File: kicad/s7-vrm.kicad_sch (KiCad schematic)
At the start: 33 parts, among them J1 Conn_02x15_Row_Letter_First, Q1 Q_NPN_BEC, Q2 Q_NMOS_GDS, Q3 Q_NMOS_GDS, SW1 SW_DIP_x04, U1 NCP1579

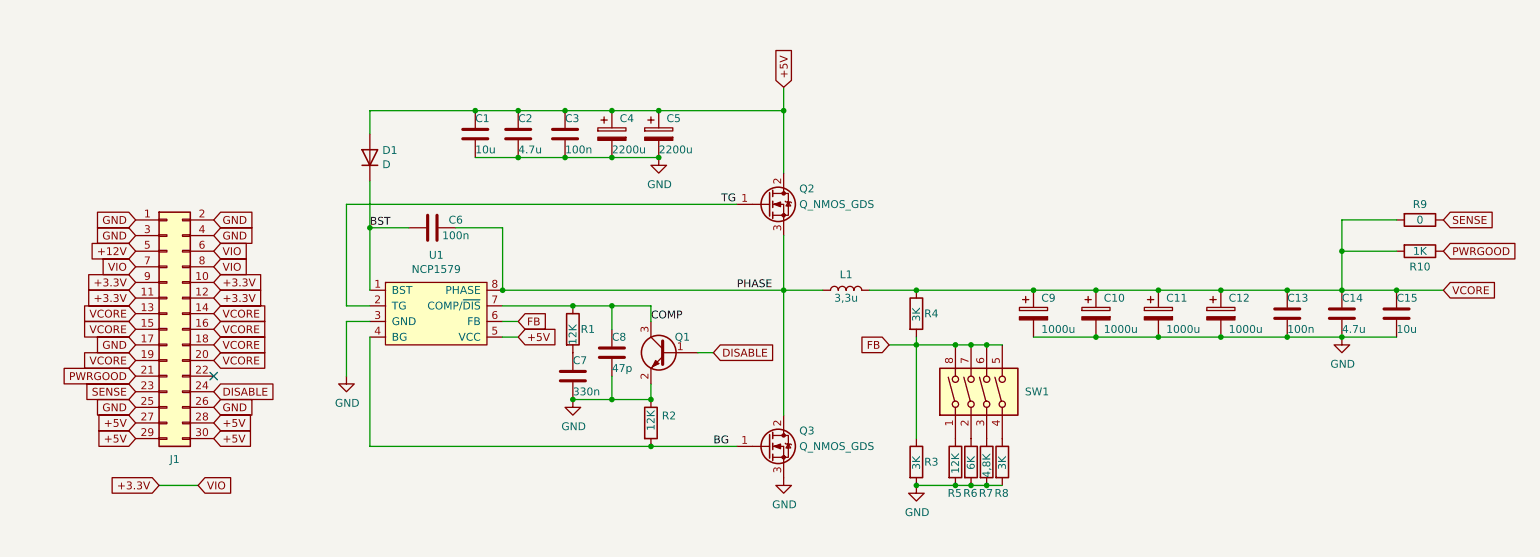
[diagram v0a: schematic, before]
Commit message: Using sence to FB and transistor for PWRGOOD
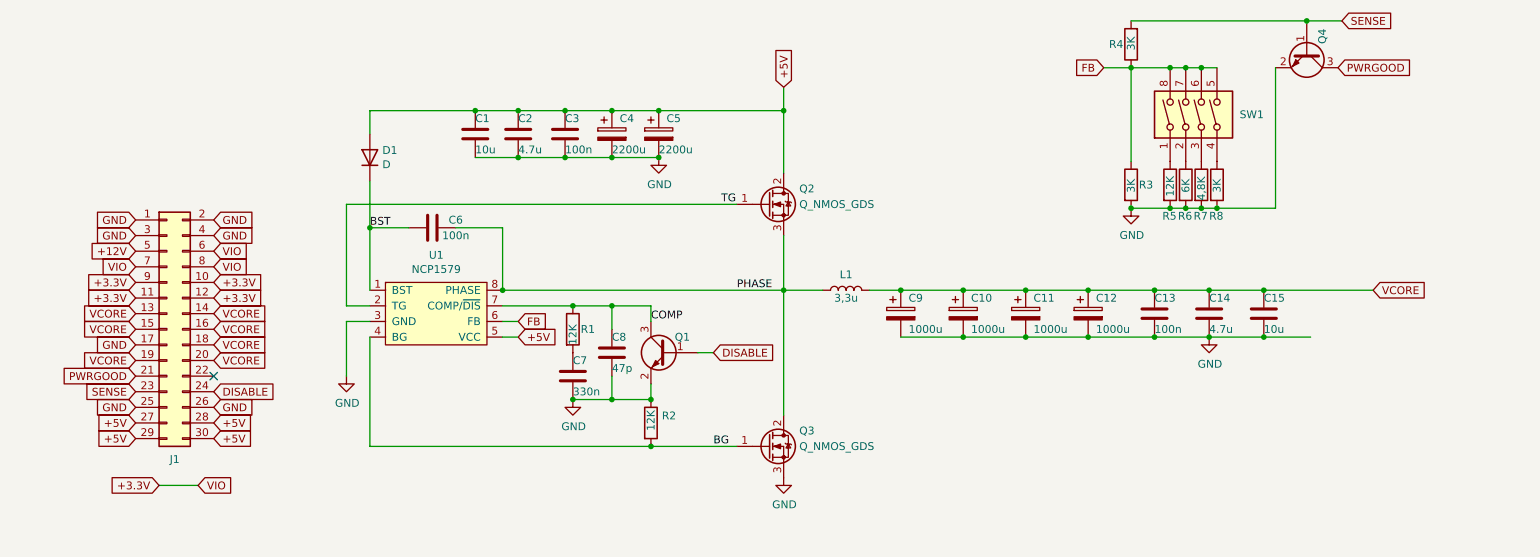
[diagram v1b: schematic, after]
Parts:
- removed R10: 1K, Resistor_SMD:R_1206_3216Metric_Pad1.30x1.75mm_HandSolder, symbol Device:R
- removed R9: 0, Resistor_SMD:R_1206_3216Metric_Pad1.30x1.75mm_HandSolder, symbol Device:R
- added Q4: Q_NPN_BEC, Package_TO_SOT_SMD:SOT-23, symbol Device:Q_NPN_BEC
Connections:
- net FB: now also R4.1; no longer R4.2
- net GND: now also Q4.2 (E)
- net PWRGOOD: now also Q4.3 (C)
- net SENSE: now also R4.2, Q4.1 (B)
- net VCORE: no longer R4.1
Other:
- moved on the sheet: C10, C11, C12, C13, C14, C15, C9, R3, R4, R5, R6, R7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

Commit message: Work in progress
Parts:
- removed Q4: Q_NPN_BEC, Package_TO_SOT_SMD:SOT-23, symbol Device:Q_NPN_BEC
- added Q4: Q_PNP_BEC_BRT, Package_TO_SOT_SMD:SOT-23, symbol Device:Q_PNP_BEC_BRT
- Q1: value Q_NPN_BEC -> Q_NPN_BEC_BRT; symbol Device:Q_NPN_BEC -> Device:Q_NPN_BEC_BRT
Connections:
- net FB: now also R4.2; no longer R4.1
- net GND: now also Q4.2 (E)
- net PWRGOOD: now also Q4.3 (C)
- net SENSE: now also R4.1; no longer R4.2
- net VCORE: now also Q4.1 (B)
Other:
- moved on the sheet: C1, C10, C11, C12, C13, C14, C15, C2, C3, C4, C5, C6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

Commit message: Prepared for production
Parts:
- C7: value 330n -> 242n; LCSC C274377 -> C107186
- C8: value 47p -> 39p; LCSC C107176 -> C577176
- R1, R2, R5: value 12K -> 15K; LCSC C2930406 -> C136874
- R3: value 3K -> 5K; LCSC C229609 -> C870818
- R4: LCSC C229609 -> C132648
- R6: value 6K -> 7,5K; LCSC C3000586 -> C137115
- R7: value 4,8K -> 6K; LCSC C488840 -> C870859
- R8: value 3K -> 3,75K; LCSC C229609 -> C706412
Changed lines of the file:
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@@
       (effects (font (size 1.27 1.27)) (justify left))
     )
-    (property "Value" "3K" (at 222.25 113.665 90)
+    (property "Value" "5K" (at 222.25 113.665 90)
       (effects (font (size 1.27 1.27)) (justify left))
     )
@@
       (effects (font (size 1.27 1.27)) hide)
     )
-    (property "LCSC" "C229609" (at 222.25 114.935 0)
+    (property "LCSC" "C870818" (at 222.25 114.935 0)
       (effects (font (size 1.27 1.27)) hide)
     )
@@
       (effects (font (size 1.27 1.27)) hide)
     )
-    (property "LCSC" "C229609" (at 245.745 133.985 0)
+    (property "LCSC" "C132648" (at 245.745 133.985 0)
       (effects (font (size 1.27 1.27)) hide)
     )
@@
       (effects (font (size 1.27 1.27)) (justify left))
     )
-    (property "Value" "4,8K" (at 233.68 112.395 90)
+    (property "Value" "6K" (at 233.68 113.665 90)
       (effects (font (size 1.27 1.27)) (justify left))
     )
@@
       (effects (font (size 1.27 1.27)) hide)
     )
-    (property "LCSC" "C488840" (at 233.68 114.935 0)
+    (property "LCSC" "C870859" (at 233.68 114.935 0)
       (effects (font (size 1.27 1.27)) hide)
     )
@@
       (effects (font (size 1.27 1.27)) (justify left))
     )
-    (property "Value" "6K" (at 231.14 113.665 90)
+    (property "Value" "7,5K" (at 231.14 112.395 90)
       (effects (font (size 1.27 1.27)) (justify left))
     )
@@
       (effects (font (size 1.27 1.27)) hide)
     )
-    (property "LCSC" "C3000586" (at 231.14 114.935 0)
+    (property "LCSC" "C137115" (at 231.14 114.935 0)
       (effects (font (size 1.27 1.27)) hide)
     )
@@
       (effects (font (size 1.27 1.27)) (justify left))
     )
-    (property "Value" "12K" (at 228.6 113.03 90)
+    (property "Value" "15K" (at 228.6 112.395 90)
       (effects (font (size 1.27 1.27)) (justify left))
     )
@@
       (effects (font (size 1.27 1.27)) hide)
     )
-    (property "LCSC" "C2930406" (at 228.6 114.935 0)
+    (property "LCSC" "C136874" (at 228.6 114.935 0)
       (effects (font (size 1.27 1.27)) hide)
     )
@@
       (effects (font (size 1.27 1.27)) (justify left))
     )
-    (property "Value" "47p" (at 116.205 109.22 0)
+    (property "Value" "39p" (at 116.205 109.22 0)
       (effects (font (size 1.27 1.27)) (justify left))
     )
@@
       (effects (font (size 1.27 1.27)) hide)
     )
-    (property "LCSC" "C107176" (at 116.205 106.68 0)
+    (property "LCSC" "C577176" (at 116.205 106.68 0)
       (effects (font (size 1.27 1.27)) hide)
     )
@@
       (effects (font (size 1.27 1.27)) (justify left))
     )
-    (property "Value" "330n" (at 109.855 113.03 0)
+    (property "Value" "242n" (at 109.855 113.03 0)
       (effects (font (size 1.27 1.27)) (justify left))
     )
@@
       (effects (font (size 1.27 1.27)) hide)
     )
-    (property "LCSC" "C274377" (at 109.855 110.49 0)
+    (property "LCSC" "C107186" (at 109.855 110.49 0)
       (effects (font (size 1.27 1.27)) hide)
     )
@@
       (effects (font (size 1.27 1.27)) (justify left))
     )
-    (property "Value" "12K" (at 109.855 105.41 90)
+    (property "Value" "15K" (at 109.855 104.775 90)
       (effects (font (size 1.27 1.27)) (justify left))
     )
@@
       (effects (font (size 1.27 1.27)) hide)
     )
-    (property "LCSC" "C2930406" (at 109.855 102.87 0)
+    (property "LCSC" "C136874" (at 109.855 102.87 0)
       (effects (font (size 1.27 1.27)) hide)
     )
@@
       (effects (font (size 1.27 1.27)) (justify left))
     )
-    (property "Value" "3K" (at 236.22 113.665 90)
+    (property "Value" "3,75K" (at 236.22 111.76 90)
       (effects (font (size 1.27 1.27)) (justify left))
     )
@@
       (effects (font (size 1.27 1.27)) hide)
     )
-    (property "LCSC" "C229609" (at 236.22 114.935 0)
+    (property "LCSC" "C706412" (at 236.22 114.935 0)
       (effects (font (size 1.27 1.27)) hide)
     )
@@
       (effects (font (size 1.27 1.27)) (justify left))
     )
-    (property "Value" "12K" (at 122.555 119.38 90)
+    (property "Value" "15K" (at 122.555 120.015 90)
       (effects (font (size 1.27 1.27)) (justify left))
     )
@@
       (effects (font (size 1.27 1.27)) hide)
     )
-    (property "LCSC" "C2930406" (at 122.555 118.11 0)
-      (effects (font (size 1.27 1.27)) hide)
-    )
+    (property "LCSC" "C136874" (at 122.555 118.11 0)
+      (effects (font (size 1.27 1.27)) hide)
+    )

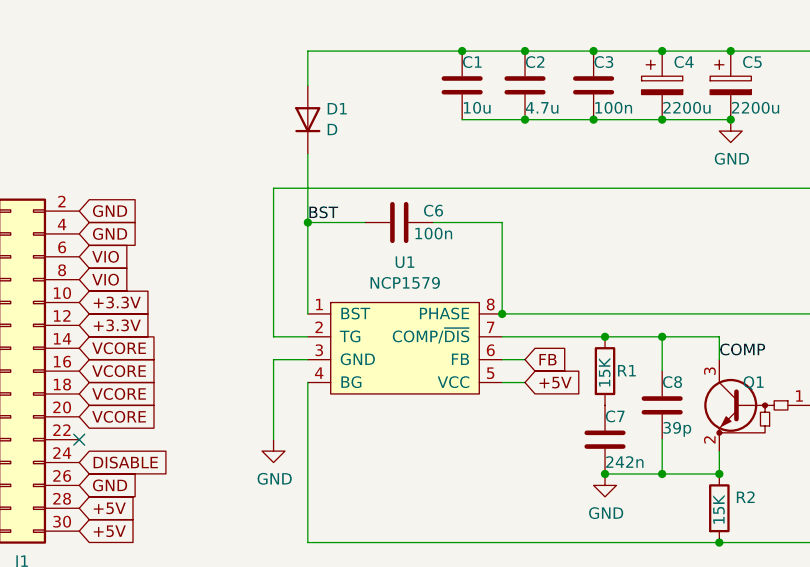
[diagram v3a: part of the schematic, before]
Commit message: Update LCSC parts and values
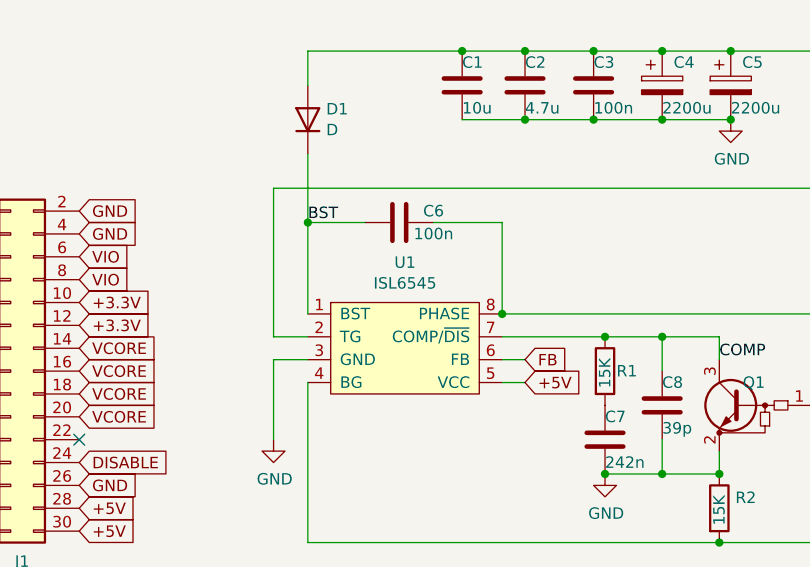
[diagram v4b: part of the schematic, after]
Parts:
- U1: value NCP1579 -> ISL6545; LCSC C235991 -> C382017
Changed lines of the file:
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@@
       (effects (font (size 1.27 1.27)))
     )
-    (property "Value" "NCP1579" (at 87.63 93.1164 0)
+    (property "Value" "ISL6545" (at 87.63 93.1164 0)
       (effects (font (size 1.27 1.27)))
     )
@@
       (effects (font (size 1.27 1.27)) hide)
     )
-    (property "LCSC" "C235991" (at 86.995 93.98 0)
+    (property "LCSC" "C382017" (at 86.995 93.98 0)
       (effects (font (size 1.27 1.27)) hide)
     )

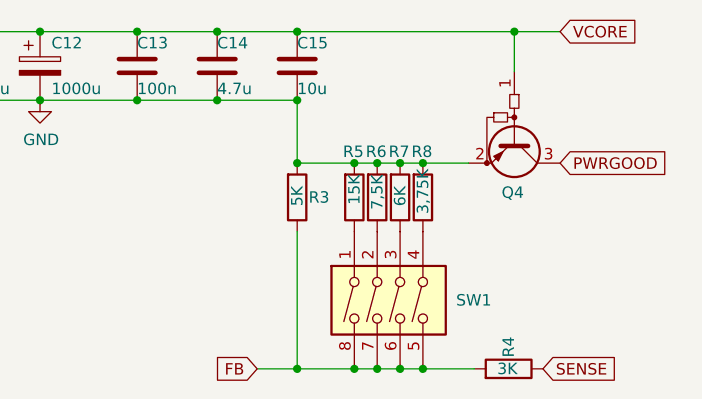
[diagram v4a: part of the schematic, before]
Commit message: Swap R3 and R4 to get proper voltage
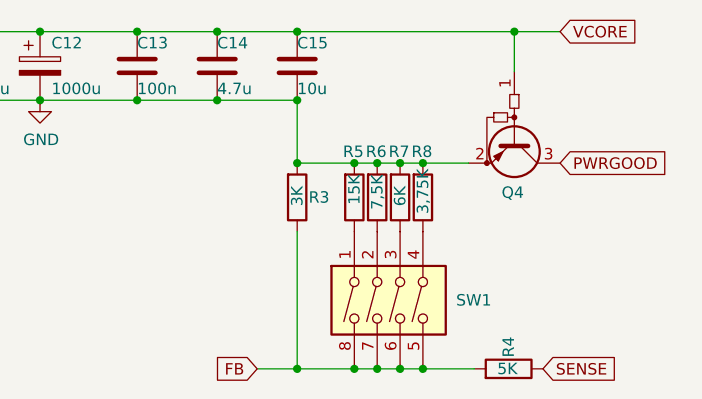
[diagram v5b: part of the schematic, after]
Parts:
- R3: value 5K -> 3K; LCSC C870818 -> C132648
- R4: value 3K -> 5K; LCSC C132648 -> C870818

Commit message: prepare rev 0.6
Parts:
- added J2: Conn_02x02_Odd_Even, Connector_PinHeader_2.54mm:PinHeader_2x02_P2.54mm_Vertical, symbol Connector_Generic:Conn_02x02_Odd_Even
- added R9: 3,75K, Resistor_SMD:R_1206_3216Metric_Pad1.30x1.75mm_HandSolder, symbol Device:R
- R3: value 3K -> 3,75K; LCSC C132648 -> C706412
- R5: value 15K -> 30K; LCSC C136874 -> C137314
- R6: value 7,5K -> 15K; LCSC C137115 -> C136874
- R7: value 6K -> 7,5K; LCSC C870859 -> C137115
- SW1: footprint Button_Switch_THT:SW_DIP_SPSTx04_Slide_9.78x12.34mm_W7.62mm_P2.54mm -> Button_Switch_THT:SW_DIP_SPSTx05_Slide_9.78x14.88mm_W7.62mm_P2.54mm; symbol Switch:SW_DIP_x04 -> Switch:SW_DIP_x05; LCSC C15781 -> C5299506
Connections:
- net +3.3V: now also J2.1 (Pin_1), J2.3 (Pin_3); no longer J1.6 (Pin_6), J1.7 (Pin_7), J1.8 (Pin_8)
- net FB: now also SW1.10, SW1.9; no longer SW1.5
- net GND: now also R9.2
- new net: R9.1, SW1.5
- new net VIO: J1.6 (Pin_6), J1.7 (Pin_7), J1.8 (Pin_8), J2.2 (Pin_2), J2.4 (Pin_4)
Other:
- moved on the sheet: Q4, R3, R4, R5, R6, R7, R8

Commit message: updated readme and bom
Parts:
- SW1: value SW_DIP_x04 -> SW_DIP_x05
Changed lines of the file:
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@@
 			)
 		)
-		(property "Value" "SW_DIP_x04"
+		(property "Value" "SW_DIP_x05"
 			(at 247.65 128.27 90)
 			(effects

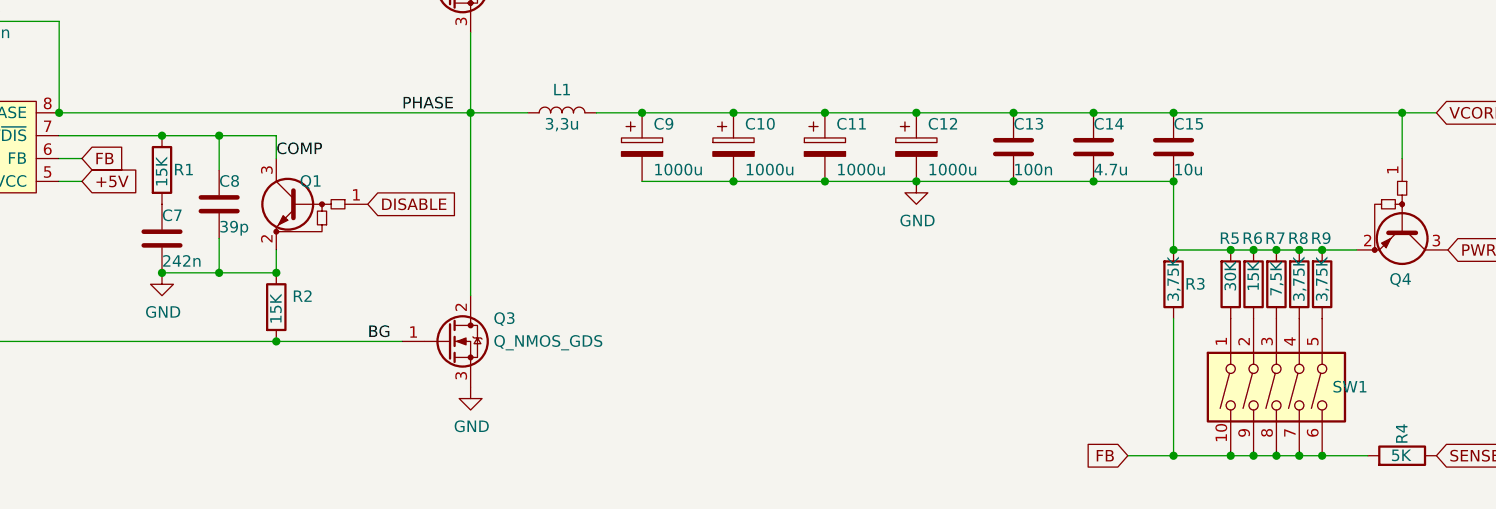
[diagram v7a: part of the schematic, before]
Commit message: Update component values based on LCSC numbers, add Gerber notes.
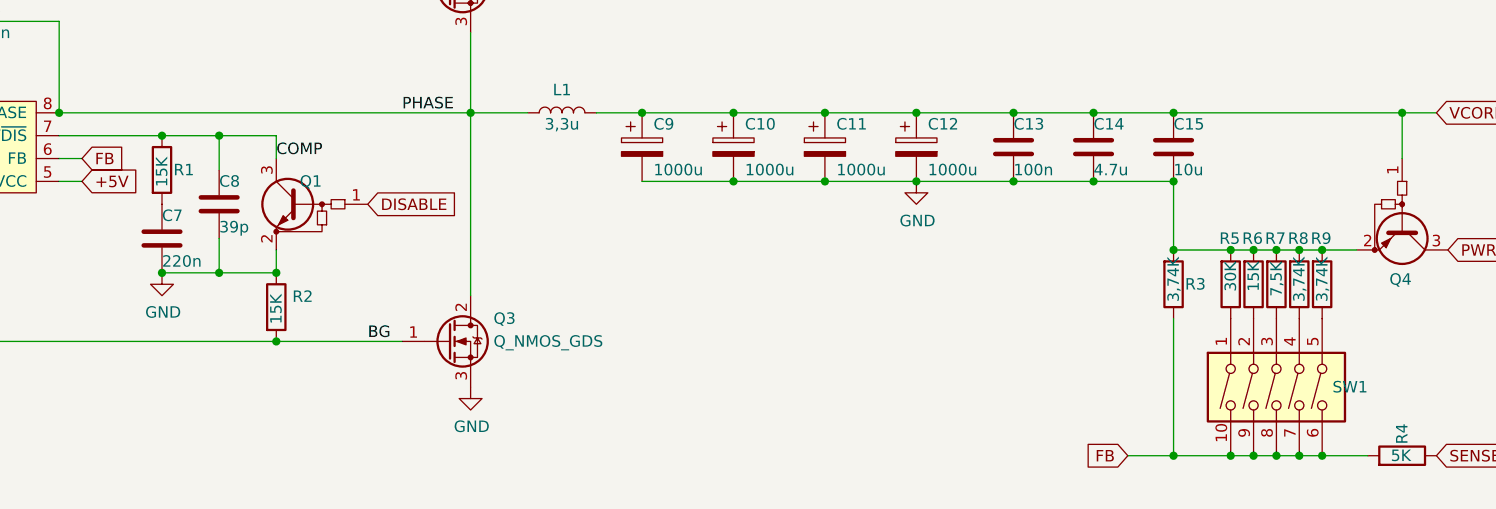
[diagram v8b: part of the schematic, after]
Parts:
- C7: value 242n -> 220n
- R3, R8, R9: value 3,75K -> 3,74K
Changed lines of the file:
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@@
 			)
 		)
-		(property "Value" "3,75K"
+		(property "Value" "3,74K"
 			(at 222.25 112.522 90)
 			(effects
@@
 			)
 		)
-		(property "Value" "242n"
+		(property "Value" "220n"
 			(at 109.855 113.03 0)
 			(effects
@@
 			)
 		)
-		(property "Value" "3,75K"
+		(property "Value" "3,74K"
 			(at 236.22 112.522 90)
 			(effects
@@
 		)
 		(instances
-			(project ""
+			(project "s7-vrm"
 				(path "/30f15357-ce1d-48b9-93dc-7d9b1b2aa048"
 					(reference "J2")
@@
 			)
 		)
-		(property "Value" "3,75K"
+		(property "Value" "3,74K"
 			(at 238.76 112.522 90)
 			(effects
